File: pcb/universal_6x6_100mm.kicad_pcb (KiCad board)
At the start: 2 copper layers, 100 x 100 mm, 80 parts

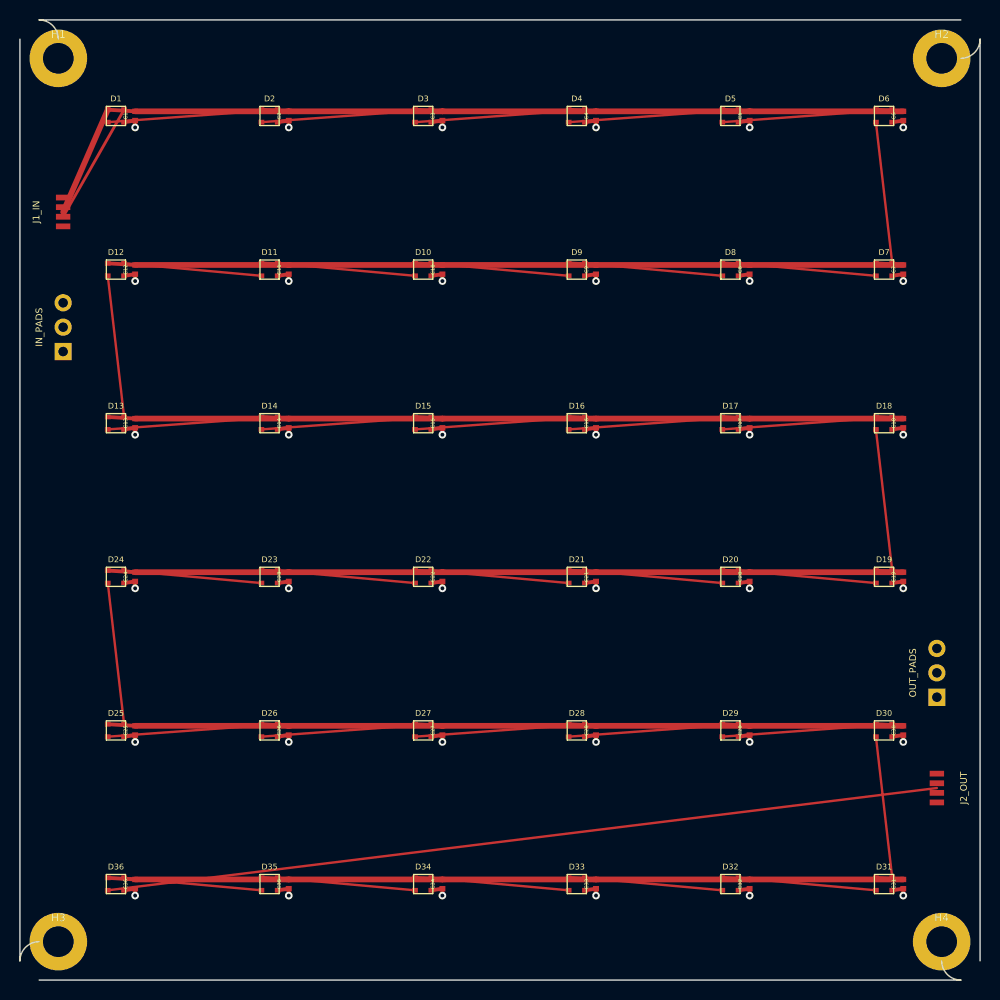
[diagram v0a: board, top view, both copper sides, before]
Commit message: feat: implement staggered offset brick rows for universal 100mm x 100mm 6x6 LED matrix
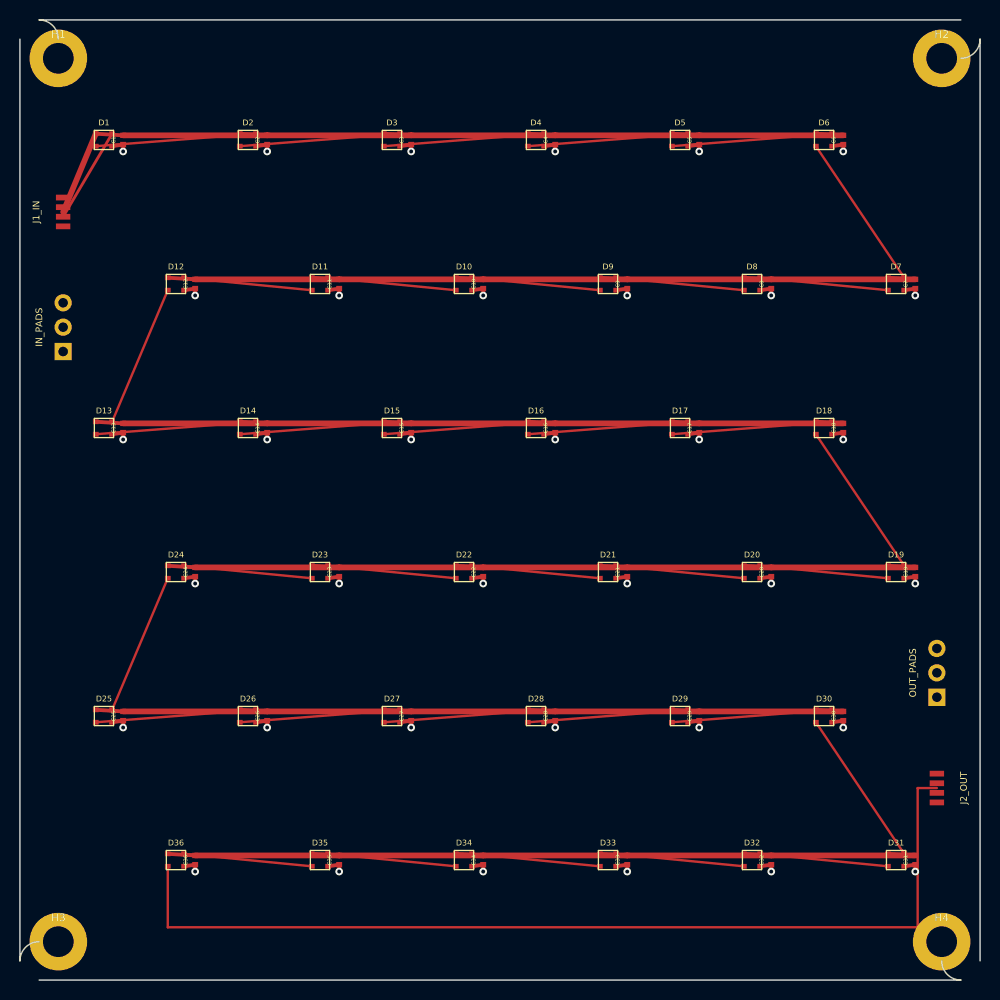
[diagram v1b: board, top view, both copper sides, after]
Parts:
- moved C36 6.73 mm to (18.2, 87.5)
- moved C6 6.73 mm to (85.8, 12.5)
- moved D36 6.73 mm to (16.2, 87.5)
- moved D6 6.73 mm to (83.8, 12.5)
- moved C12 6.43 mm to (18.2, 27.5)
- moved C30 6.43 mm to (85.8, 72.5)
- moved D12 6.43 mm to (16.2, 27.5)
- moved D30 6.43 mm to (83.8, 72.5)
- moved C18 6.27 mm to (85.8, 42.5)
- moved C24 6.27 mm to (18.2, 57.5)
- moved D18 6.27 mm to (83.8, 42.5)
- moved D24 6.27 mm to (16.2, 57.5)
- moved C35 5.81 mm to (33.2, 87.5)
- moved C5 5.81 mm to (70.8, 12.5)
- moved D35 5.81 mm to (31.2, 87.5)
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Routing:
- net +5V: track 594.4 -> 561.6 mm
- net DATA_37: track 87.0 -> 100.9 mm
- net DATA_1: track 12.8 -> 10.0 mm
- net DATA_31: track 14.8 -> 16.5 mm
- net DATA_7: track 14.8 -> 16.5 mm
- net DATA_19: track 14.8 -> 16.5 mm
- net DATA_6: track 17.7 -> 16.8 mm
- net DATA_5: track 17.7 -> 16.8 mm
- net DATA_4: track 17.7 -> 16.8 mm
- net DATA_30: track 17.7 -> 16.8 mm
- net DATA_3: track 17.7 -> 16.8 mm
- net DATA_29: track 17.7 -> 16.8 mm
- net DATA_28: track 17.7 -> 16.8 mm
- net DATA_27: track 17.7 -> 16.8 mm
- net DATA_26: track 17.7 -> 16.8 mm
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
